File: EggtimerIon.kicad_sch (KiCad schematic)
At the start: 6 parts, among them U1 ESP32-WROOM-32-N4, U2 MPU-6050, U3 MS5611-01BA, U4 CAT24C512XI-T2, U5 AP2112K-3.3

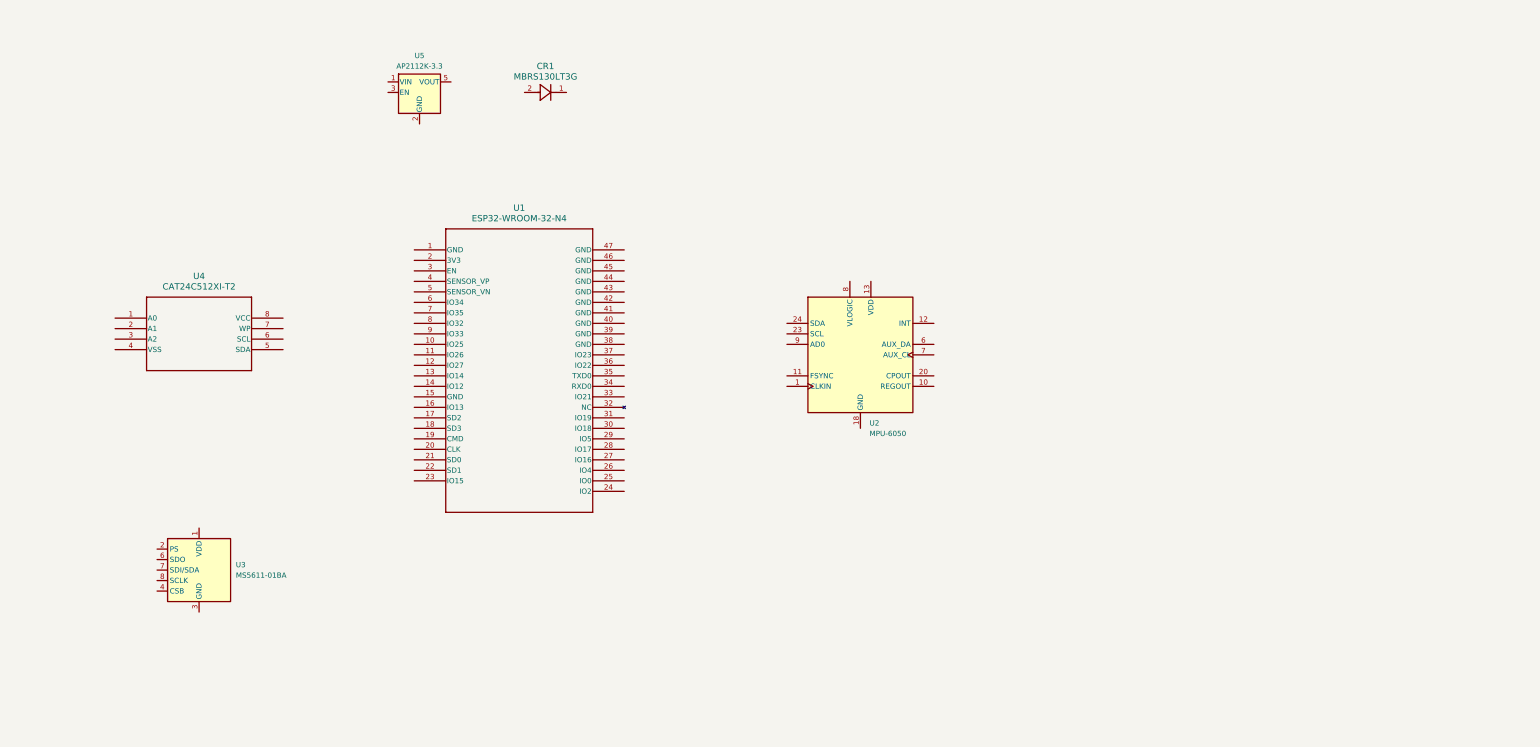
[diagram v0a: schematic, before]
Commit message: ESP32-WROOM Connections
Labelled all pins on module
Added elementary connections and jumpers
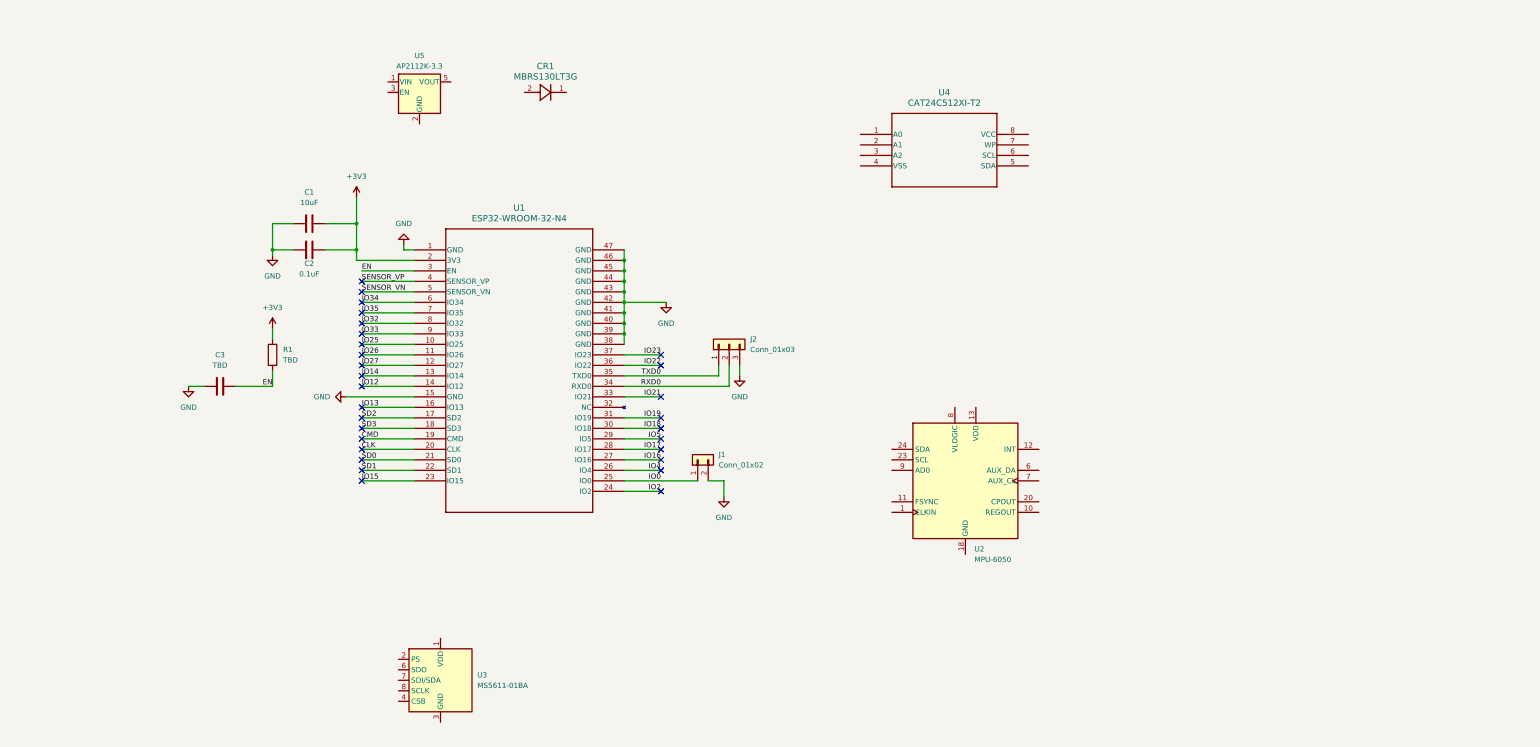
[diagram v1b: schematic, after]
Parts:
- added C1: 10uF, symbol Device:C
- added C2: 0.1uF, symbol Device:C
- added C3: TBD, symbol Device:C
- added J1: Conn_01x02, symbol Connector_Generic:Conn_01x02
- added J2: Conn_01x03, symbol Connector_Generic:Conn_01x03
- added R1: TBD, symbol Device:R
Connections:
- net GND: now reaches U1.1 (GND)
- net GND: now also U1.15 (GND), U1.38 (GND), U1.39 (GND), U1.40 (GND), U1.41 (GND), U1.42 (GND), U1.43 (GND), U1.44 (GND), U1.45 (GND), U1.46 (GND), U1.47 (GND), C1.1, C2.1, C3.1, J1.2 (Pin_2), J2.3 (Pin_3)
- net IO25: now reaches U1.10 (IO25)
- net IO26: now reaches U1.11 (IO26)
- net IO27: now reaches U1.12 (IO27)
- net IO14: now reaches U1.13 (IO14)
- net IO12: now reaches U1.14 (IO12)
- net IO13: now reaches U1.16 (IO13)
- net SD2: now reaches U1.17 (SD2)
- net SD3: now reaches U1.18 (SD3)
- net CMD: now reaches U1.19 (CMD)
- net +3V3: now reaches U1.2 (3V3)
- net +3V3: now also C1.2, C2.2, R1.1
- net CLK: now reaches U1.20 (CLK)
- net SD0: now reaches U1.21 (SD0)
- net SD1: now reaches U1.22 (SD1)
- net IO15: now reaches U1.23 (IO15)
- net IO2: now reaches U1.24 (IO2)
- net IO0: now reaches U1.25 (IO0)
- net IO0: now also J1.1 (Pin_1)
- net IO4: now reaches U1.26 (IO4)
- net IO16: now reaches U1.27 (IO16)
- net IO17: now reaches U1.28 (IO17)
- net IO5: now reaches U1.29 (IO5)
- net EN: now reaches U1.3 (EN)
- net EN: now also C3.2, R1.2
- net IO18: now reaches U1.30 (IO18)
- net IO19: now reaches U1.31 (IO19)
- net IO21: now reaches U1.33 (IO21)
- net RXD0: now reaches U1.34 (RXD0)
- net RXD0: now also J2.2 (Pin_2)
- net TXD0: now reaches U1.35 (TXD0)
- net TXD0: now also J2.1 (Pin_1)
- net IO22: now reaches U1.36 (IO22)
- net IO23: now reaches U1.37 (IO23)
- net SENSOR_VP: now reaches U1.4 (SENSOR_VP)
- net SENSOR_VN: now reaches U1.5 (SENSOR_VN)
- net IO34: now reaches U1.6 (IO34)
- net IO35: now reaches U1.7 (IO35)
- net IO32: now reaches U1.8 (IO32)
- net IO33: now reaches U1.9 (IO33)
- no-connect marks 0 -> 29
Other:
- moved on the sheet: U2, U3, U4

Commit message: MPU6050 Connections
Modified IO22 and IO23 on ESP for I2C lines
Added capacitors and followed general application note for IMU
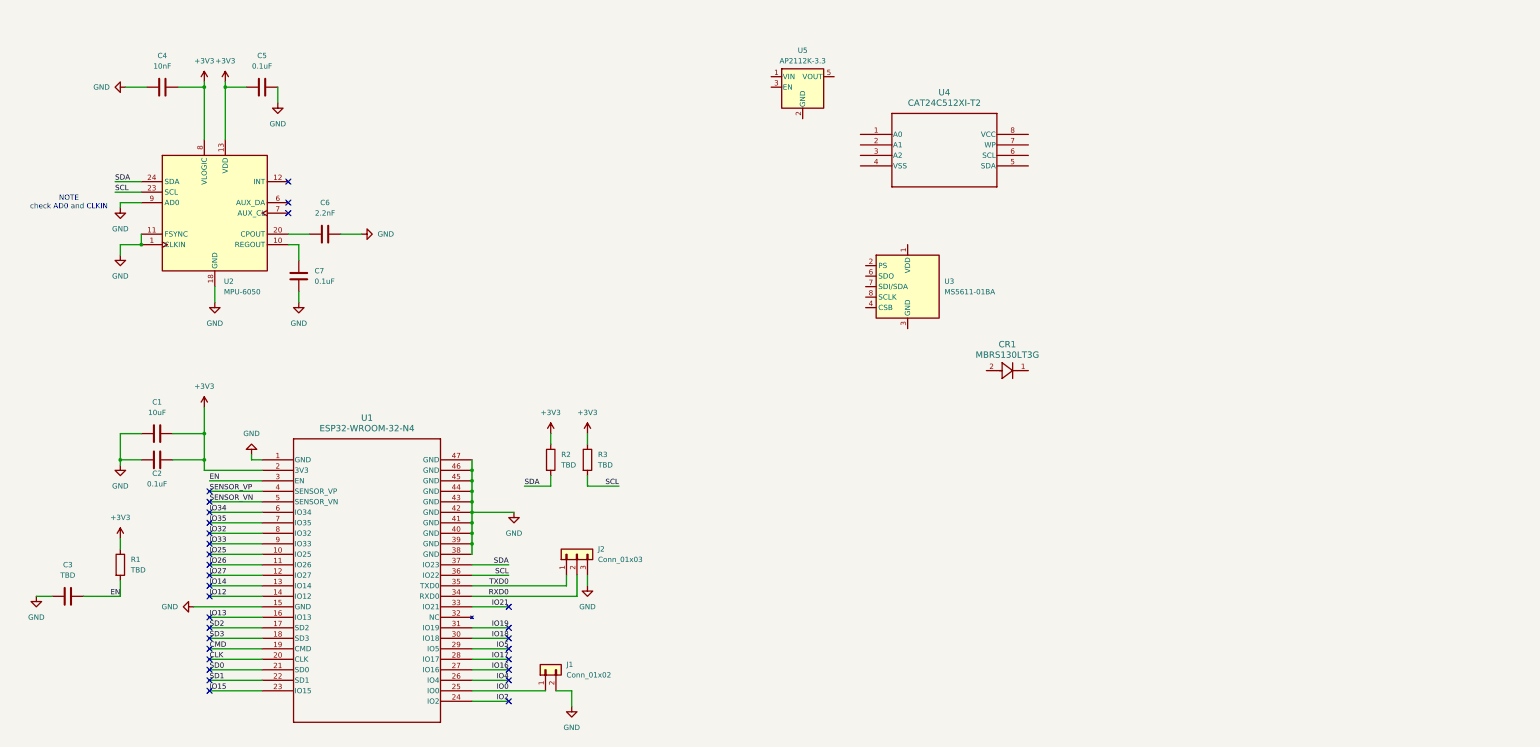
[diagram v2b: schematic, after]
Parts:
- added C4: 10nF, symbol Device:C
- added C5, C7: 0.1uF, symbol Device:C
- added C6: 2.2nF, symbol Device:C
- added R2, R3: TBD, symbol Device:R
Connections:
- net IO22 is gone; now on net SCL: U1.36 (IO22)
- net IO23 is gone; now on net SDA: U1.37 (IO23)
- net +3V3: now also U2.13 (VDD), U2.8 (VLOGIC), C4.2, C5.2, R2.1, R3.1
- net GND: now also U2.1 (CLKIN), U2.11 (FSYNC), U2.18 (GND), U2.9 (AD0), C4.1, C5.1, C6.2, C7.2
- net at U2.10 (REGOUT): now also C7.1
- net at U2.20 (CPOUT): now also C6.1
- net SCL: now reaches U2.23 (SCL)
- net SCL: now also R3.2
- net SDA: now reaches U2.24 (SDA)
- net SDA: now also R2.2
- no-connect marks 29 -> 30
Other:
- note added: "NOTE check AD0 and CLKIN"
- moved on the sheet: C1, C2, C3, CR1, J1, J2, R1, U1, U2, U3, U5

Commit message: MS6511 Connections
Added capacitors and connected MS5611 to ESP
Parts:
- added C8: 100nF, symbol Device:C
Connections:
- net +3V3: now also U3.1 (VDD), U3.2 (PS), C8.1
- net GND: now also U3.3 (GND), C8.2
- net SCL: now also U3.8 (SCLK)
- net SDA: now also U3.7 (SDI/SDA)
- no-connect marks 30 -> 32
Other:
- note added: "check CSB"
- note added: "might be 10K as per MS5611 datasheet"
- moved on the sheet: U3

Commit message: CAT24C512 Connections
Connected EEPROM module to to ESP
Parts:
- added C9: 0.1uF, symbol Device:C
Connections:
- net +3V3: now also U4.8 (VCC), C9.1
- net GND: now also U4.1 (A0), U4.2 (A1), U4.3 (A2), U4.4 (VSS), U4.7 (WP), C9.2
- net SCL: now also U4.6 (SCL)
- net SDA: now also U4.5 (SDA)
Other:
- moved on the sheet: CR1, U4, U5

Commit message: Buzzer, LDO, and JST connected
Added connections for LDO, JST, and Buzzer (with NFET) to ESP
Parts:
- added C10, C11: 1uF, symbol Device:C
- added J3: B2B-PH-K-S, B2B-PH-K-S:JST_B2B-PH-K-S, symbol B2B-PH-K-S:B2B-PH-K-S
- added LS1: AT-1127-ST-2-R, AT-1127-ST-2-R:XDCR_AT-1127-ST-2-R, symbol AT-1127-ST-2-R:AT-1127-ST-2-R
- added Q1: IRLML6244, Package_TO_SOT_SMD:SOT-23, symbol Transistor_FET:IRLML6244
- added R4: R, symbol Device:R
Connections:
- net +3V3: now also U5.5 (VOUT), C11.1, R4.1
- net GND: now also U5.2 (GND), C10.2, C11.2, Q1.2 (S)
- net IO18: now also Q1.1 (G)
- net at U5.1 (VIN): now also CR1.1
- net BAT+: now reaches CR1.2
- net BAT+: now also C10.1, J3.1
- new net: LS1.P, R4.2
- new net: LS1.N, Q1.3 (D)
- new net BAT-: J3.2
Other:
- moved on the sheet: C8, CR1, U3, U5

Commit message: Assigned Footprints
annotated schematic
assigned footprints
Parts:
- C1, C10, C11, C2, C3, C4, C5, C6, C7, C8, C9: footprint (none) -> PCM_JLCPCB:C_1206
- CR1: footprint DIODE_SMB_2L_ONS -> MBRS130L3TG:DIODE_SMB_2L_ONS
- J1: footprint (none) -> Connector_PinHeader_2.54mm:PinHeader_1x02_P2.54mm_Vertical
- J2: footprint (none) -> Connector_PinHeader_2.54mm:PinHeader_1x03_P2.54mm_Vertical
- R1, R2, R3, R4: footprint (none) -> PCM_JLCPCB:R_1206
- U1: footprint MOD_ESP32-WROOM-32_EXP -> ESP32-WROOM-32-N4:MOD_ESP32-WROOM-32_EXP
- U4: footprint SOIC8_ONS -> CAT24C512:SOIC8_ONS
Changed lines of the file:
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@@
 			)
 		)
-		(property "Footprint" ""
+		(property "Footprint" "PCM_JLCPCB:R_1206"
 			(at 230.632 90.17 90)
 			(effects
@@
 			)
 		)
-		(property "Footprint" ""
+		(property "Footprint" "PCM_JLCPCB:R_1206"
 			(at 40.132 147.32 90)
 			(effects
@@
 			)
 		)
-		(property "Footprint" "DIODE_SMB_2L_ONS"
+		(property "Footprint" "MBRS130L3TG:DIODE_SMB_2L_ONS"
 			(at 191.77 26.67 0)
 			(effects
@@
 			)
 		)
-		(property "Footprint" ""
+		(property "Footprint" "PCM_JLCPCB:R_1206"
 			(at 144.272 121.92 90)
 			(effects
@@
 			)
 		)
-		(property "Footprint" ""
+		(property "Footprint" "PCM_JLCPCB:C_1206"
 			(at 33.02 153.9748 0)
 			(effects
@@
 			)
 		)
-		(property "Footprint" ""
+		(property "Footprint" "Connector_PinHeader_2.54mm:PinHeader_1x02_P2.54mm_Vertical"
 			(at 144.78 172.72 0)
 			(effects
@@
 			)
 		)
-		(property "Footprint" ""
+		(property "Footprint" "Connector_PinHeader_2.54mm:PinHeader_1x03_P2.54mm_Vertical"
 			(at 152.4 144.78 0)
 			(effects
@@
 			)
 		)
-		(property "Footprint" ""
+		(property "Footprint" "PCM_JLCPCB:C_1206"
 			(at 95.25 66.3448 0)
 			(effects
@@
 			)
 		)
-		(property "Footprint" "MOD_ESP32-WROOM-32_EXP"
+		(property "Footprint" "ESP32-WROOM-32-N4:MOD_ESP32-WROOM-32_EXP"
 			(at 76.2 121.92 0)
 			(effects
@@
 			)
 		)
-		(property "Footprint" ""
+		(property "Footprint" "PCM_JLCPCB:R_1206"
 			(at 153.162 121.92 90)
 			(effects
@@
 			)
 		)
-		(property "Footprint" ""
+		(property "Footprint" "PCM_JLCPCB:C_1206"
 			(at 72.39 32.7152 0)
 			(effects
@@
 			)
 		)
-		(property "Footprint" ""
+		(property "Footprint" "PCM_JLCPCB:C_1206"
 			(at 54.61 120.9548 0)
 			(effects
@@
 			)
 		)
-		(property "Footprint" ""
+		(property "Footprint" "PCM_JLCPCB:C_1206"
 			(at 186.3852 35.56 0)
 			(effects
@@
 			)
 		)
-		(property "Footprint" ""
+		(property "Footprint" "PCM_JLCPCB:C_1206"
 			(at 152.4 38.4048 0)
 			(effects
@@
 			)
 		)
-		(property "Footprint" ""
+		(property "Footprint" "PCM_JLCPCB:C_1206"
 			(at 234.6452 35.56 0)
 			(effects
@@
 			)
 		)
-		(property "Footprint" ""
+		(property "Footprint" "PCM_JLCPCB:C_1206"
 			(at 55.88 30.7848 0)
 			(effects
@@
 			)
 		)
-		(property "Footprint" ""
+		(property "Footprint" "PCM_JLCPCB:C_1206"
 			(at 86.0552 81.28 0)
 			(effects
@@
 			)
 		)
-		(property "Footprint" ""
+		(property "Footprint" "PCM_JLCPCB:C_1206"
 			(at 255.27 132.3848 0)
 			(effects
@@
 			)
 		)
-		(property "Footprint" "SOIC8_ONS"
+		(property "Footprint" "CAT24C512:SOIC8_ONS"
 			(at 200.66 139.7 0)
 			(effects
@@
 			)
 		)
-		(property "Footprint" ""
+		(property "Footprint" "PCM_JLCPCB:C_1206"
 			(at 54.61 114.6048 0)
 			(effects

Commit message: Initialized footprint
Assigned some LCSC part numbers
Need to update ESP32 footprint to THT
Need to setup 4 layer board settings
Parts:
- U1: LCSC (none) -> C82899
- U3: LCSC (none) -> C15639
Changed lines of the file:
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@@
 	(title_block
 		(title "Eggtimer Ion Flight Computer ")
-		(date "2025-10-02")
+		(date "2025-10-06")
 		(rev "v1.0")
 		(company "Metropolitan Aerospace Rocket Society")
@@
 			)
 		)
+		(property "LCSC" "C15639"
+			(at 142.24 55.88 0)
+			(effects
+				(font
+					(size 1.27 1.27)
+				)
+				(hide yes)
+			)
+		)
 		(pin "5"
 		)
@@
 			(at 76.2 121.92 0)
 			(effects
+				(font
+					(size 1.27 1.27)
+				)
+				(hide yes)
+			)
+		)
+		(property "LCSC" "C82899"
+			(at 76.2 121.92 0)
+			(effects

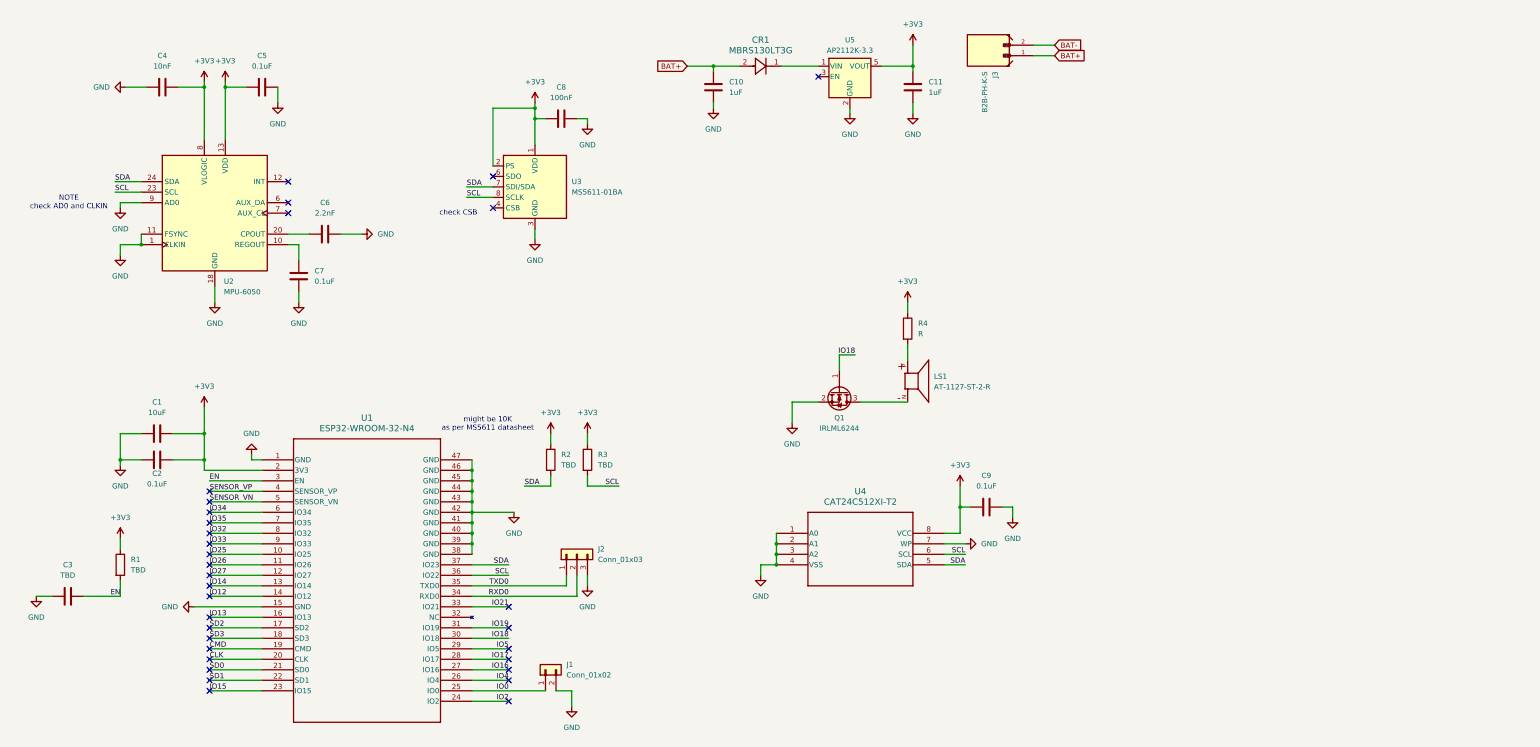
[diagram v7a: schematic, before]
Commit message: Added USB C connections
Added USB C Receptacle
Added USB to UART bridge
Added external circuitry for CP2102N module
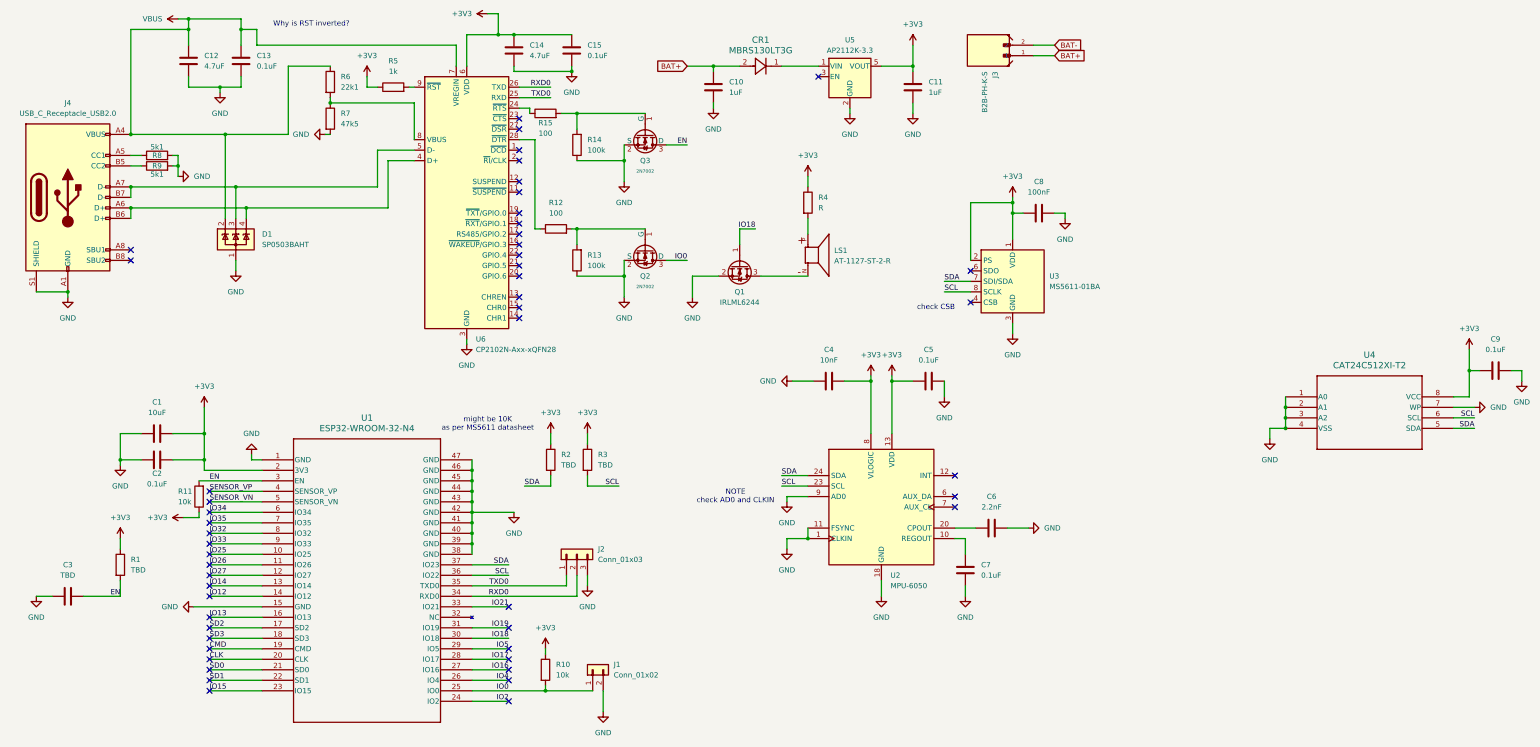
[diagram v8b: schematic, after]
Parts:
- added C12, C14: 4.7uF, PCM_JLCPCB:C_1206, symbol Device:C
- added C13, C15: 0.1uF, PCM_JLCPCB:C_1206, symbol Device:C
- added D1: SP0503BAHT, Package_TO_SOT_SMD:SOT-143, symbol Power_Protection:SP0503BAHT
- added J4: USB_C_Receptacle_USB2.0, Connector_USB:USB_C_Receptacle_G-Switch_GT-USB-7010ASV, symbol USBCCOnn:USB_C_Receptacle_USB2.0
- added Q2, Q3: 2N7002, PCM_JLCPCB:Q_SOT-23, symbol PCM_JLCPCB-Transistors:NMOS,2N7002
- added R10, R11: 10k, PCM_JLCPCB:R_1206, symbol Device:R
- added R12, R15: 100, PCM_JLCPCB:R_1206, symbol Device:R
- added R13, R14: 100k, PCM_JLCPCB:R_1206, symbol Device:R
- added R5: 1k, PCM_JLCPCB:R_1206, symbol Device:R
- added R6: 22k1, PCM_JLCPCB:R_1206, symbol Device:R
- added R7: 47k5, PCM_JLCPCB:R_1206, symbol Device:R
- added R8, R9: 5k1, PCM_JLCPCB:R_1206, symbol Device:R
- added U6: CP2102N-Axx-xQFN28, Package_DFN_QFN:QFN-28-1EP_5x5mm_P0.5mm_EP3.35x3.35mm, symbol Interface_USB:CP2102N-Axx-xQFN28
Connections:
- net +3V3: now also C14.1, C15.1, R10.1, R11.1, R5.1, U6.6 (VDD)
- net EN: now also Q3.3 (D), R11.2
- net GND: now also C12.2, C13.2, C14.2, C15.2, D1.1 (A), J4.A1 (GND), J4.A12 (GND), J4.B1 (GND), J4.B12 (GND), J4.S1 (SHIELD), Q2.2 (S), Q3.2 (S), R13.1, R14.1, R7.2, R8.2, R9.2, U6.29 (GND), U6.3 (GND)
- net IO0: now also Q2.3 (D), R10.2
- net RXD0: now also U6.26 (TXD)
- net TXD0: now also U6.25 (RXD)
- new net: D1.3 (K), J4.A7 (D-), J4.B7 (D-), U6.5 (D-)
- new net: D1.4 (K), J4.A6 (D+), J4.B6 (D+), U6.4 (D+)
- new net: J4.A5 (CC1), R8.1
- new net: Q3.1 (G), R14.2, R15.2
- new net: Q2.1 (G), R12.2, R13.2
- new net: J4.B5 (CC2), R9.1
- new net: R12.1, U6.28 (~{DTR})
- new net: R15.1, U6.24 (~{RTS})
- new net: R6.2, R7.1, U6.8 (VBUS)
- new net: R5.2, U6.9 (~{RST})
- new net VBUS: C12.1, C13.1, D1.2 (K), J4.A4 (VBUS), J4.A9 (VBUS), J4.B4 (VBUS), J4.B9 (VBUS), R6.1, U6.7 (VREGIN)
- no-connect marks 32 -> 50
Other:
- note added: "Why is RST inverted?"
- moved on the sheet: C4, C5, C6, C7, C8, C9, J1, LS1, Q1, R4, U2, U3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
